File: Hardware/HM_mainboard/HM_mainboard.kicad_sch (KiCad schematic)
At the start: 0 parts

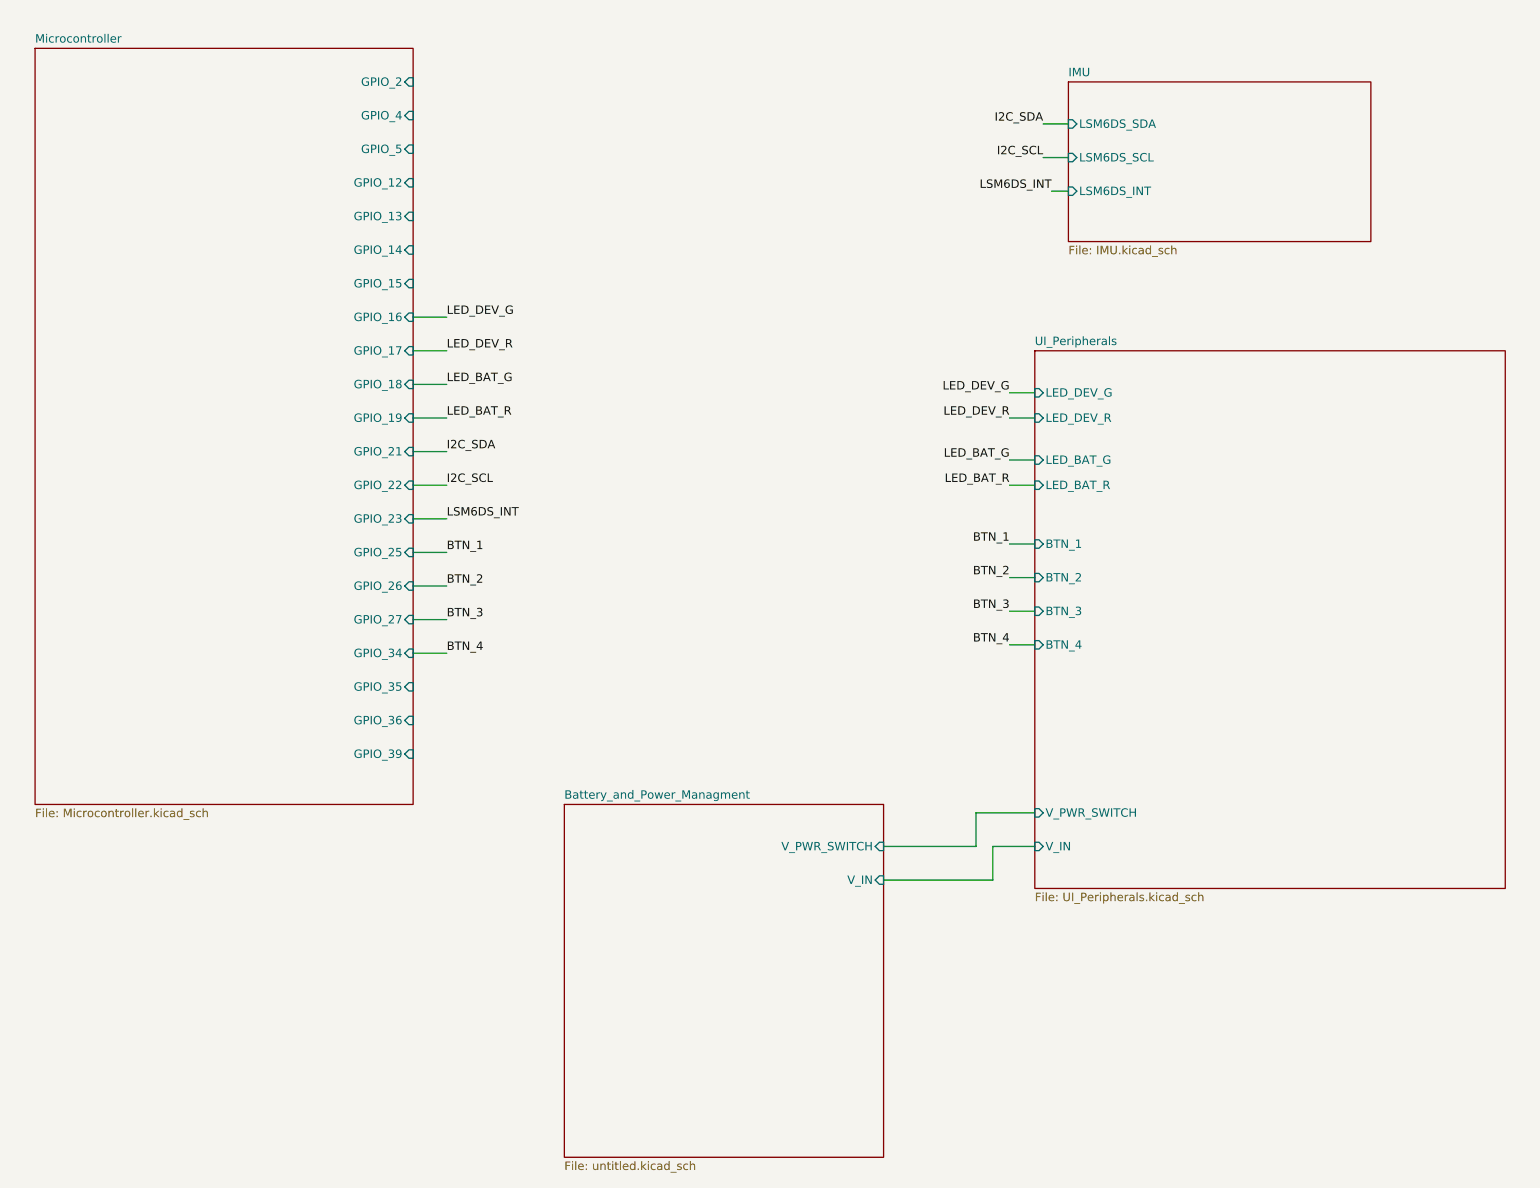
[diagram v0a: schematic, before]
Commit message: Updated port connectors to new microcontroller
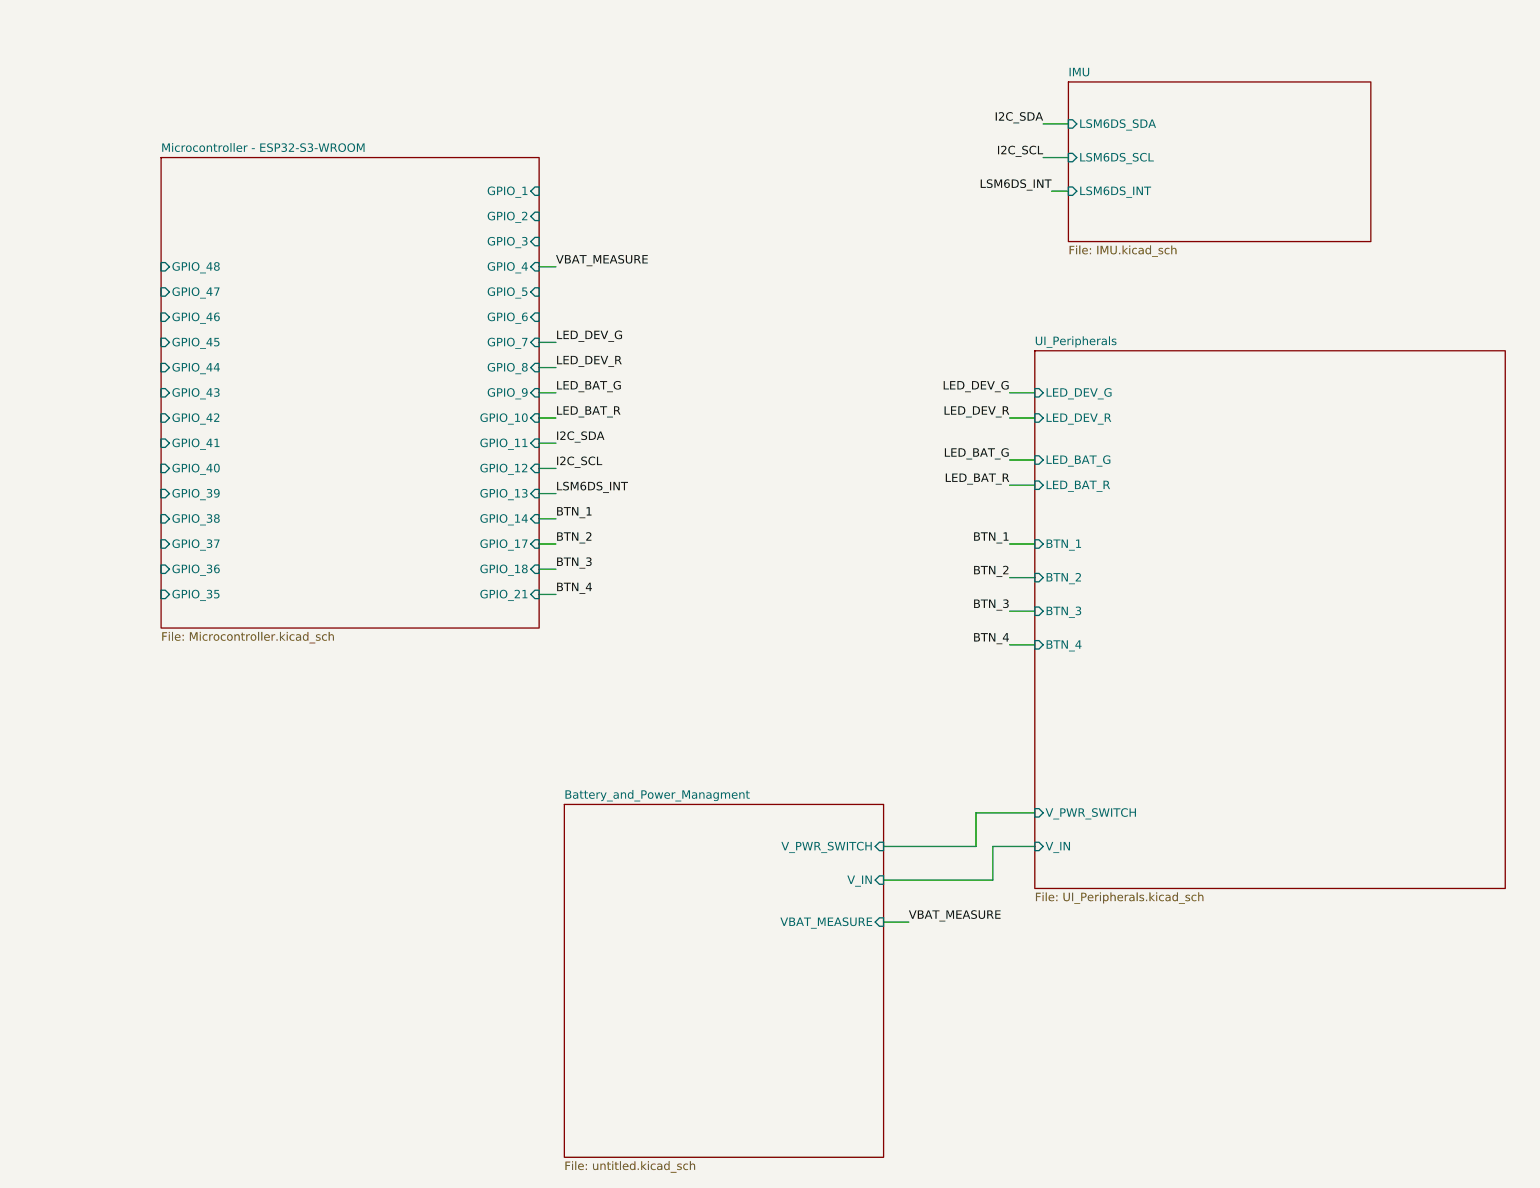
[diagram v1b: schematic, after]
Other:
- sheet Microcontroller renamed Microcontroller - ESP32-S3-WROOM
- sheet Battery_and_Power_Managment ports: added VBAT_MEASURE; removed none
- sheet Microcontroller - ESP32-S3-WROOM ports: added GPIO_1, GPIO_10, GPIO_11, GPIO_3, GPIO_37, GPIO_38, GPIO_40, GPIO_41, GPIO_42, GPIO_43, GPIO_44, GPIO_45, GPIO_46, GPIO_47, GPIO_48, GPIO_6, GPIO_7, GPIO_8, GPIO_9; removed GPIO_15, GPIO_16, GPIO_19, GPIO_22, GPIO_23, GPIO_25, GPIO_26, GPIO_27, GPIO_34

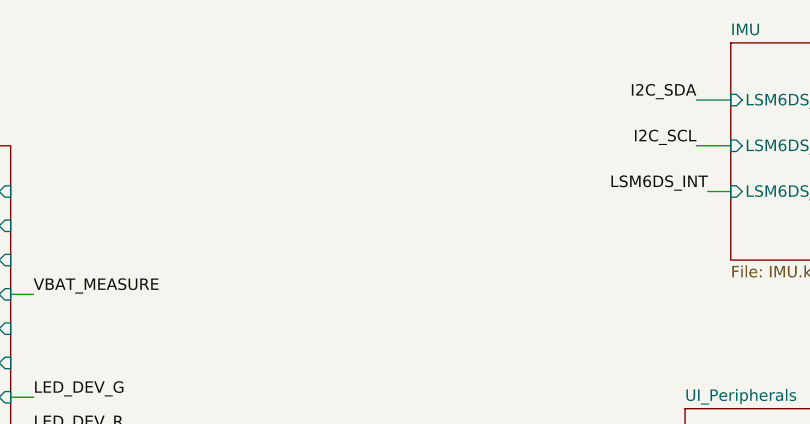
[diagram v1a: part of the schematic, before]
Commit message: Updated port connectors of microcontroller
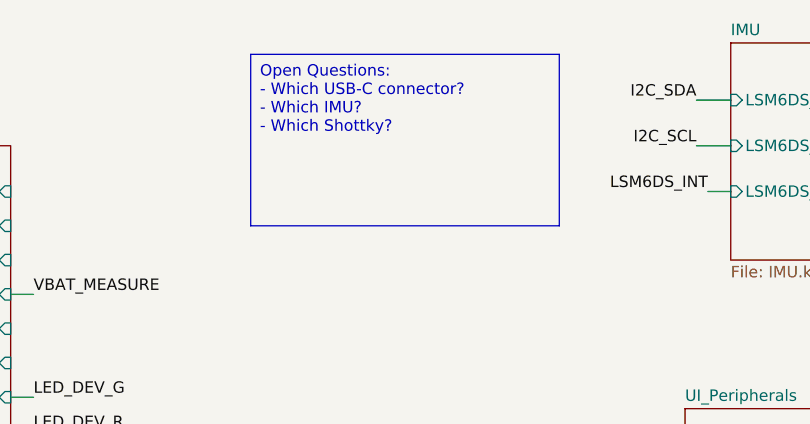
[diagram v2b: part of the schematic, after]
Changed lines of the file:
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@@
     (stroke (width 0) (type default))
+  )
+  (text_box "Open Questions:\n- Which USB-C connector?\n- Which IMU?\n- Which Shottky?"
+    (at 125.73 25.4 0) (size 34.29 19.05)
+    (stroke (width 0) (type default))
+    (fill (type none))
+    (effects (font (size 1.27 1.27)) (justify left top))
   )
   (label "LED_DEV_R" (at 101.6 67.31 0) (fields_autoplaced)

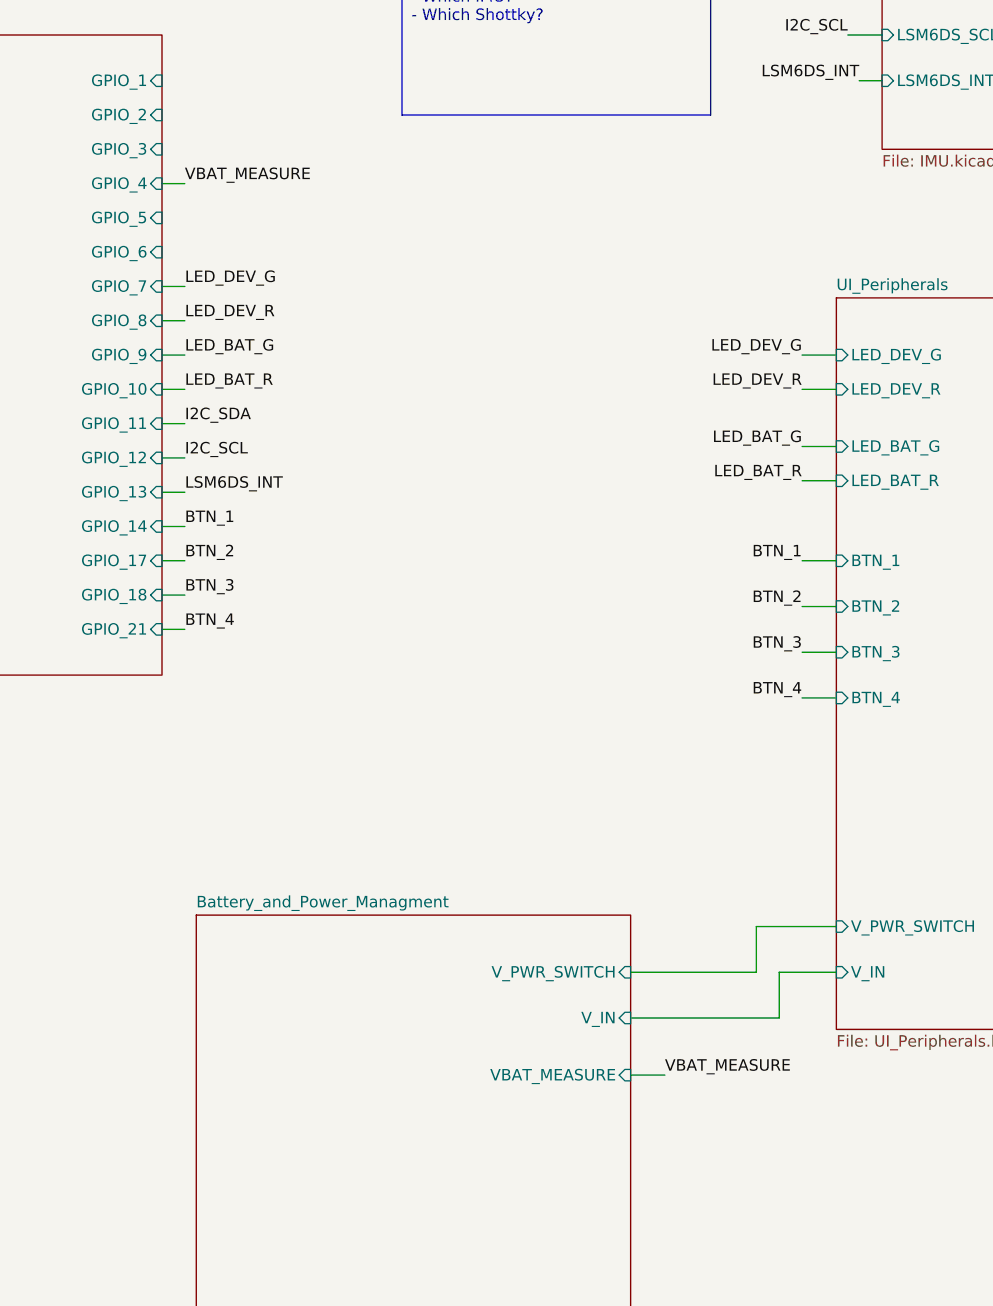
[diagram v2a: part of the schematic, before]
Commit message: Added IMUs, updated some components
- Added 2 additonal IMUs:
     1) 6-Axis MC6470
     2) 9-Axis BNO55
- Replaced button jack connectors
- Replaced battery charging LED by a charging status measurement circuit
- Replaced caps for clock crystal
- Added stabalizing caps to uC Vcc
- Added UART pin header
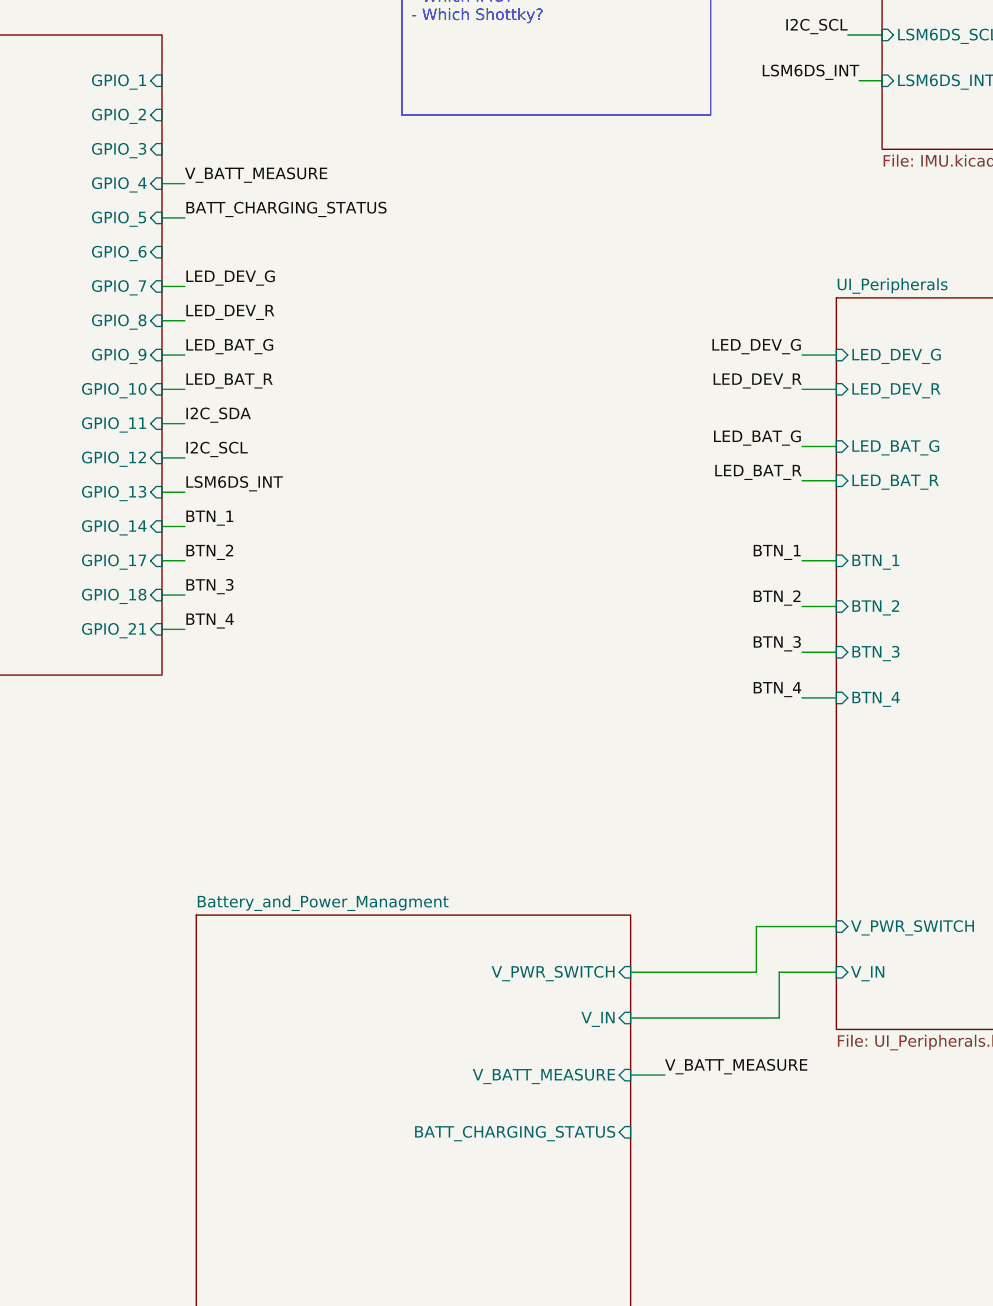
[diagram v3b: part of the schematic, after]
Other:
- sheet Battery_and_Power_Managment ports: added BATT_CHARGING_STATUS, V_BATT_MEASURE; removed VBAT_MEASURE
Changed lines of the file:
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@@
+    (stroke (width 0) (type default))
+  )
+  (wire (pts (xy 99.06 55.88) (xy 101.6 55.88))
     (stroke (width 0) (type default))
   )
@@
     (effects (font (size 1.27 1.27)) (justify left top))
   )
+  (label "BATT_CHARGING_STATUS" (at 101.6 55.88 0) (fields_autoplaced)
+    (effects (font (size 1.27 1.27)) (justify left bottom))
+  )
   (label "LED_DEV_R" (at 101.6 67.31 0) (fields_autoplaced)
     (effects (font (size 1.27 1.27)) (justify left bottom))
   )
-  (label "VBAT_MEASURE" (at 101.6 52.07 0) (fields_autoplaced)
+  (label "V_BATT_MEASURE" (at 101.6 52.07 0) (fields_autoplaced)
     (effects (font (size 1.27 1.27)) (justify left bottom))
   )
@@
     (effects (font (size 1.27 1.27)) (justify left bottom))
   )
-  (label "VBAT_MEASURE" (at 154.94 151.13 0) (fields_autoplaced)
+  (label "V_BATT_MEASURE" (at 154.94 151.13 0) (fields_autoplaced)
     (effects (font (size 1.27 1.27)) (justify left bottom))
   )
@@
       (effects (font (size 1.27 1.27)) (justify right))
     )
-    (pin "VBAT_MEASURE" input (at 151.13 151.13 0)
-      (effects (font (size 1.27 1.27)) (justify right))
-    )
+    (pin "V_BATT_MEASURE" input (at 151.13 151.13 0)
+      (effects (font (size 1.27 1.27)) (justify right))
+    )
+    (pin "BATT_CHARGING_STATUS" input (at 151.13 157.48 0)
+      (effects (font (size 1.27 1.27)) (justify right))
+    )
